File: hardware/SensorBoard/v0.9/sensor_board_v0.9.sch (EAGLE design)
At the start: 43 parts, among them IC1 BMP280, IC2 VREF, J3 USB-MICROB, U1 LMP91000, U10 CCS811, U11 RFM69HW, U2 TSL2561, U3 ATMEGA328P-MU, U7 SHT31, U8 MCP1703/3.3V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

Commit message: Corrected resistor and capacitor values for voltage ref.
Also added adjusted CCS811 tstop pads
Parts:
- C9: value 1uF -> 10uF
- R3: value 49.9 -> 1K
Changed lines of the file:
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@@
 <?xml version="1.0" encoding="utf-8"?>
 <!DOCTYPE eagle SYSTEM "eagle.dtd">
-<eagle version="7.6.0">
+<eagle version="7.7.0">
 <drawing>
 <settings>
@@
 <part name="GND6" library="SparkFun-Aesthetics" deviceset="GND" device=""/>
 <part name="C10" library="SparkFun-Passives" deviceset="CAP" device="0805" value="0.1uF"/>
-<part name="R3" library="SparkFun-Passives" deviceset="RESISTOR" device="0805-RES" value="49.9">
-<attribute name="MF" value=""/>
-<attribute name="MPN" value=""/>
-<attribute name="OC_NEWARK" value="unknown"/>
-</part>
-<part name="C9" library="SparkFun-Passives" deviceset="CAP" device="0805" value="1uF"/>
+<part name="R3" library="SparkFun-Passives" deviceset="RESISTOR" device="0805-RES" value="1K">
+<attribute name="MF" value=""/>
+<attribute name="MPN" value=""/>
+<attribute name="OC_NEWARK" value="unknown"/>
+</part>
+<part name="C9" library="SparkFun-Passives" deviceset="CAP" device="0805" value="10uF"/>
 <part name="GND11" library="SparkFun-Aesthetics" deviceset="GND" device=""/>
 <part name="SUPPLY12" library="SparkFun-Aesthetics" deviceset="VCC" device=""/>

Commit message: created BOM for version .9
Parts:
- C1, C5, C6: MPN (none) -> CC0805KKX7R7BB105; OC_NEWARK unknown -> (none)
- C10, C12, C15, C2, C7, C8: MPN (none) -> CC0603KRX7R7BB104
- C11, C3, C4: MPN (none) -> CC0603KRX7R7BB104; OC_NEWARK unknown -> (none)
- C9: MPN (none) -> CC0805ZKY5V6BB106
- IC1: MPN (none) -> BMP280
- IC2: MPN (none) -> ISL60002DIH320ZCB
- J2: NO_BOM (none) -> TRUE
- J3: MPN (none) -> CONN-09505
- LED2, RX, TX: MPN (none) -> LTST-C170TBKT; OC_NEWARK unknown -> (none)
- R1: MPN (none) -> RC0805FR-0749R9L; OC_NEWARK unknown -> (none)
- R10, R4, R9: MPN (none) -> RC0805JR-0747RL; OC_NEWARK unknown -> (none)
- R11: MPN (none) -> SD0805S020S0R5; OC_NEWARK unknown -> (none)
- R12, R21: MPN (none) -> RC0805FR-0727RL; OC_NEWARK unknown -> (none)
- R13: MPN (none) -> RC0805JR-0710KL
- R2: MPN (none) -> 311-100KCRCT-ND; OC_NEWARK unknown -> (none)
- R3: MPN (none) -> RC0805JR-071KL; OC_NEWARK unknown -> (none)
- R5, R6: MPN (none) -> RC0805JR-0710KL; OC_NEWARK unknown -> (none)
- U$1: MPN (none) -> FT231XQ-R
- U$2: MPN (none) -> 3SP CO
- U1: MPN (none) -> LMP91000
- U10: MPN (none) -> CCS811
- U11: MPN (none) -> RFM69HW
- U2: DIGIKEY# TSL2561-FNCT-ND -> (none); MANF AMS-TAOS-USA-Inc. -> (none); MANF# TSL2561FN -> (none); MOUSER# 856-TSL2561T -> (none); OC_NEWARK 82Y5564 -> (none)
- U3: MPN (none) -> ATMEGA328P-MU
- U7: OC_NEWARK 47Y1304 -> (none)
- U8: OC_NEWARK 18T9177 -> (none)
- X1: MPN (none) -> WRL-00593
- Y1: MPN (none) -> CSTCE16M0V53-R0; OC_NEWARK unknown -> (none)

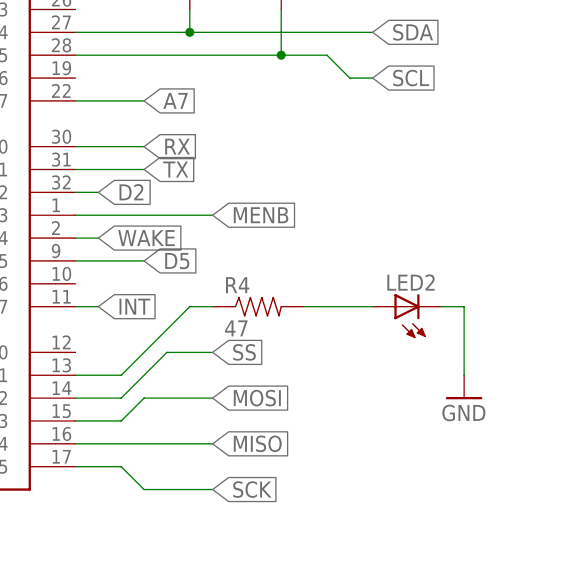
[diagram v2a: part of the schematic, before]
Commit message: updated LED descriptions
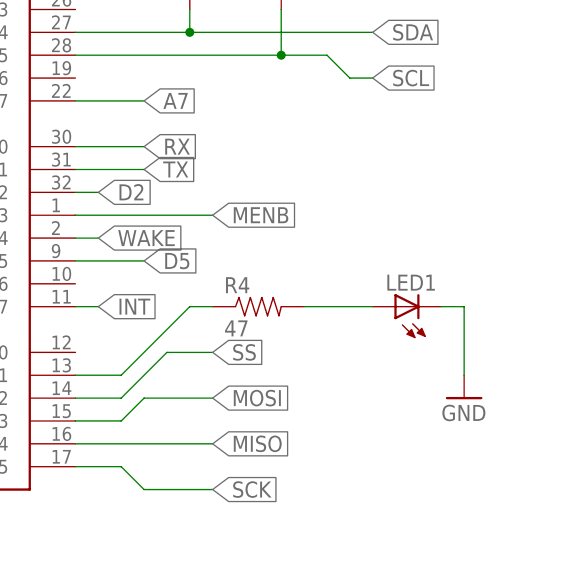
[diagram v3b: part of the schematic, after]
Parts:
- C10, C11, C12, C15, C2, C3, C4, C7, C8: MPN CC0603KRX7R7BB104 -> AC0805KRX7R9BB104
- IC2: MPN ISL60002DIH320ZCB -> ISL60002DIH320Z-TK
- LED1: MPN LTST-C170TBKT -> 150080BS75000
- RX: MPN LTST-C170TBKT -> LG R971-KN-1
- TX: MPN LTST-C170TBKT -> LH R974-LP-1
- renumbered LED2 to LED1
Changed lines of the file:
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@@
 </part>
 <part name="C3" library="SparkFun-Passives" deviceset="CAP" device="0805" value="0.1uF">
-<attribute name="MPN" value="CC0603KRX7R7BB104"/>
+<attribute name="MPN" value="AC0805KRX7R9BB104"/>
 </part>
 <part name="C4" library="SparkFun-Passives" deviceset="CAP" device="0805" value="0.1uF">
-<attribute name="MPN" value="CC0603KRX7R7BB104"/>
+<attribute name="MPN" value="AC0805KRX7R9BB104"/>
 </part>
 <part name="Y1" library="SparkFun-FreqCtrl" deviceset="RESONATOR" device="16MHZ" value="16MHZ">
@@
 </part>
 <part name="SUPPLY7" library="SparkFun-Aesthetics" deviceset="VCC" device=""/>
-<part name="LED2" library="adafruit" deviceset="LED" device="CHIPLED_0805">
-<attribute name="MPN" value="LTST-C170TBKT"/>
+<part name="LED1" library="adafruit" deviceset="LED" device="CHIPLED_0805">
+<attribute name="MPN" value="150080BS75000"/>
 </part>
 <part name="GND8" library="SparkFun-Aesthetics" deviceset="GND" device=""/>
@@
 </part>
 <part name="C12" library="SparkFun-Passives" deviceset="CAP" device="0805" value="0.1uF">
-<attribute name="MPN" value="CC0603KRX7R7BB104"/>
+<attribute name="MPN" value="AC0805KRX7R9BB104"/>
 </part>
 <part name="SUPPLY11" library="SparkFun-Aesthetics" deviceset="VCC" device=""/>
@@
 </part>
 <part name="RX" library="adafruit" deviceset="LED" device="CHIPLED_0805" value="Green">
-<attribute name="MPN" value="LTST-C170TBKT"/>
+<attribute name="MPN" value="LG R971-KN-1"/>
 </part>
 <part name="TX" library="adafruit" deviceset="LED" device="CHIPLED_0805" value="Red">
-<attribute name="MPN" value="LTST-C170TBKT"/>
+<attribute name="MPN" value="LH R974-LP-1"/>
 </part>
 <part name="R9" library="SparkFun-Passives" deviceset="RESISTOR" device="0805-RES" value="47">
@@
 </part>
 <part name="C11" library="SparkFun-Capacitors" deviceset="CAP" device="0805" value="0.1uF">
-<attribute name="MPN" value="CC0603KRX7R7BB104"/>
+<attribute name="MPN" value="AC0805KRX7R9BB104"/>
 </part>
 <part name="GND7" library="SparkFun-Aesthetics" deviceset="GND" device=""/>
@@
 </part>
 <part name="C15" library="SparkFun-Passives" deviceset="CAP" device="0805" value="0.1uF">
-<attribute name="MPN" value="CC0603KRX7R7BB104"/>
+<attribute name="MPN" value="AC0805KRX7R9BB104"/>
 </part>
 <part name="U10" library="CCS811" deviceset="CCS811" device="-I2C" value="CCS811">
@@
 <part name="SUPPLY6" library="SparkFun-Aesthetics" deviceset="VCC" device=""/>
 <part name="C2" library="SparkFun-Passives" deviceset="CAP" device="0805" value="0.1uF">
-<attribute name="MPN" value="CC0603KRX7R7BB104"/>
+<attribute name="MPN" value="AC0805KRX7R9BB104"/>
 </part>
 <part name="C8" library="SparkFun-Passives" deviceset="CAP" device="0805" value="0.1uF">
-<attribute name="MPN" value="CC0603KRX7R7BB104"/>
+<attribute name="MPN" value="AC0805KRX7R9BB104"/>
 </part>
 <part name="U3" library="ATMEGA328P-MU" deviceset="ATMEGA328P-MU" device="">
@@
 <part name="SUPPLY9" library="SparkFun-Aesthetics" deviceset="VCC" device=""/>
 <part name="C7" library="SparkFun-Passives" deviceset="CAP" device="0805" value="0.1uF">
-<attribute name="MPN" value="CC0603KRX7R7BB104"/>
+<attribute name="MPN" value="AC0805KRX7R9BB104"/>
 </part>
 <part name="IC2" library="linear" deviceset="ISL60002DIH320Z" device="CB" value="VREF">
-<attribute name="MPN" value="ISL60002DIH320ZCB"/>
+<attribute name="MPN" value="ISL60002DIH320Z-TK"/>
 </part>
 <part name="GND6" library="SparkFun-Aesthetics" deviceset="GND" device=""/>
 <part name="C10" library="SparkFun-Passives" deviceset="CAP" device="0805" value="0.1uF">
-<attribute name="MPN" value="CC0603KRX7R7BB104"/>
+<attribute name="MPN" value="AC0805KRX7R9BB104"/>
 </part>
 <part name="R3" library="SparkFun-Passives" deviceset="RESISTOR" device="0805-RES" value="1K">
@@
 </instance>
 <instance part="SUPPLY7" gate="G$1" x="345.44" y="129.54"/>
-<instance part="LED2" gate="G$1" x="363.22" y="78.74" rot="R90">
+<instance part="LED1" gate="G$1" x="363.22" y="78.74" rot="R90">
 <attribute name="MPN" x="363.22" y="78.74" size="1.778" layer="96" rot="R270" display="off"/>
 </instance>
@@
 </segment>
 <segment>
-<pinref part="LED2" gate="G$1" pin="C"/>
+<pinref part="LED1" gate="G$1" pin="C"/>
 <pinref part="GND8" gate="1" pin="GND"/>
 <wire x1="368.3" y1="78.74" x2="370.84" y2="78.74" width="0.1524" layer="91"/>
@@
 <segment>
 <pinref part="R4" gate="G$1" pin="2"/>
-<pinref part="LED2" gate="G$1" pin="A"/>
+<pinref part="LED1" gate="G$1" pin="A"/>
 <wire x1="353.06" y1="78.74" x2="360.68" y2="78.74" width="0.1524" layer="91"/>
 </segment>
